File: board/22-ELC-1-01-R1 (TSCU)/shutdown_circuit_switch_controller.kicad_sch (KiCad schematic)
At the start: 28 parts, among them Q5 AO3400A, Q6 AO3400A, Q7 SUD50P04-09L-E3, Q8 SUD50P04-09L-E3, U11 SN74LVC1G14DBV, U12 74LS32, U3 74HC74D,653, U4 SGM809-SXN3/TR

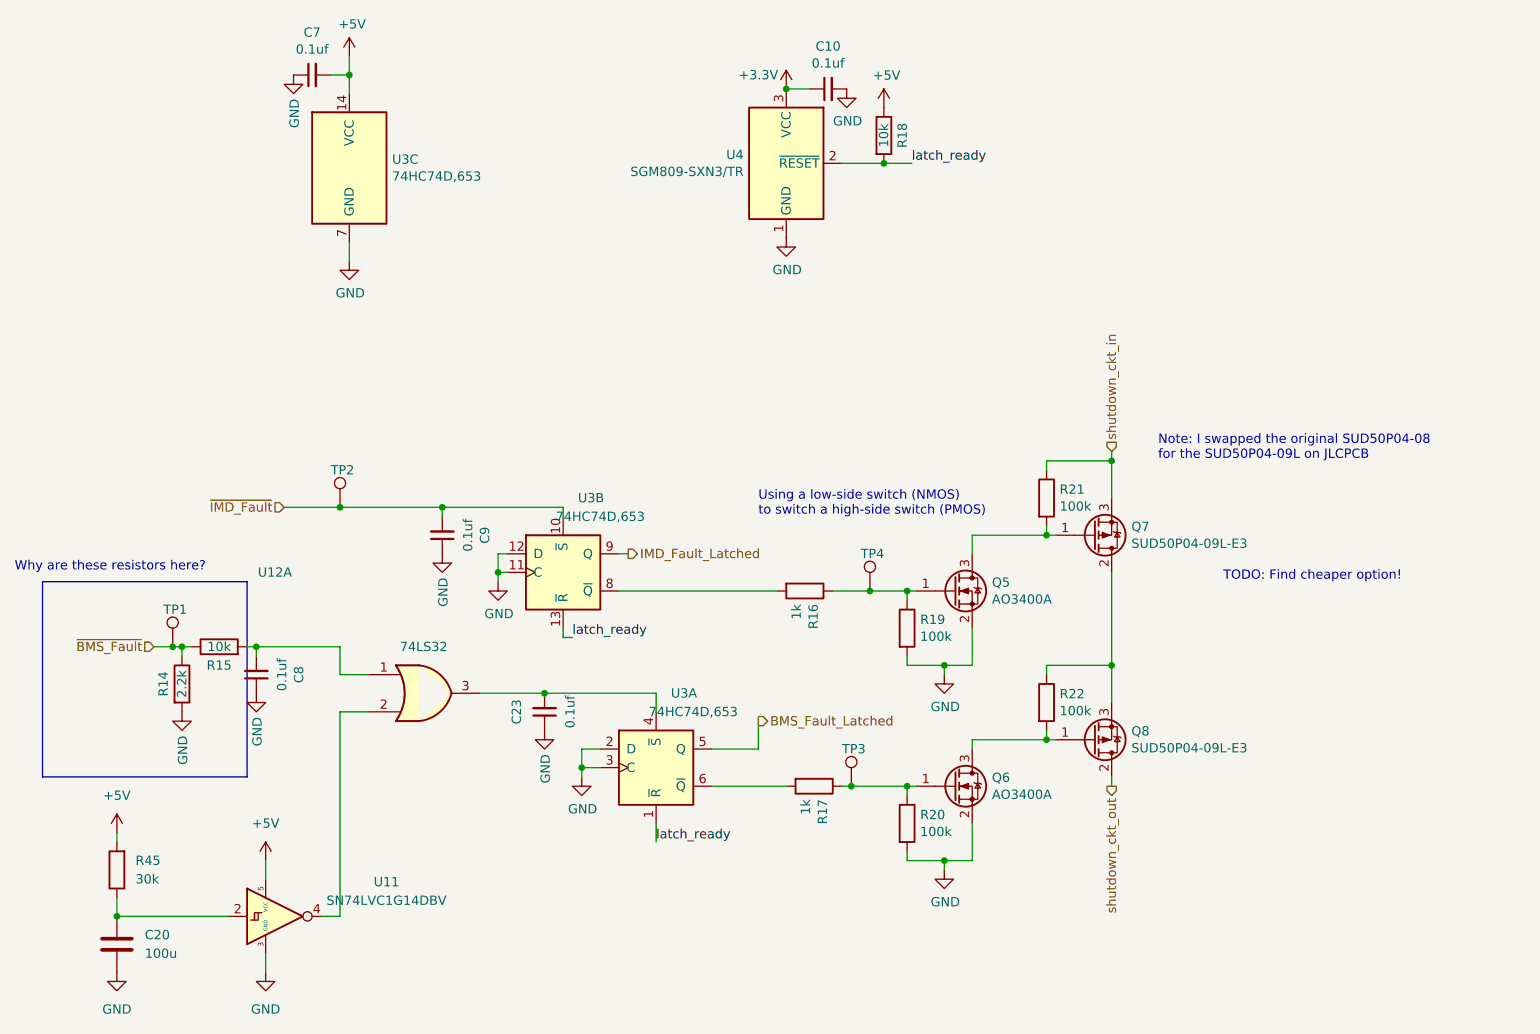
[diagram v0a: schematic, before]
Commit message: Added FAULT_RESET button
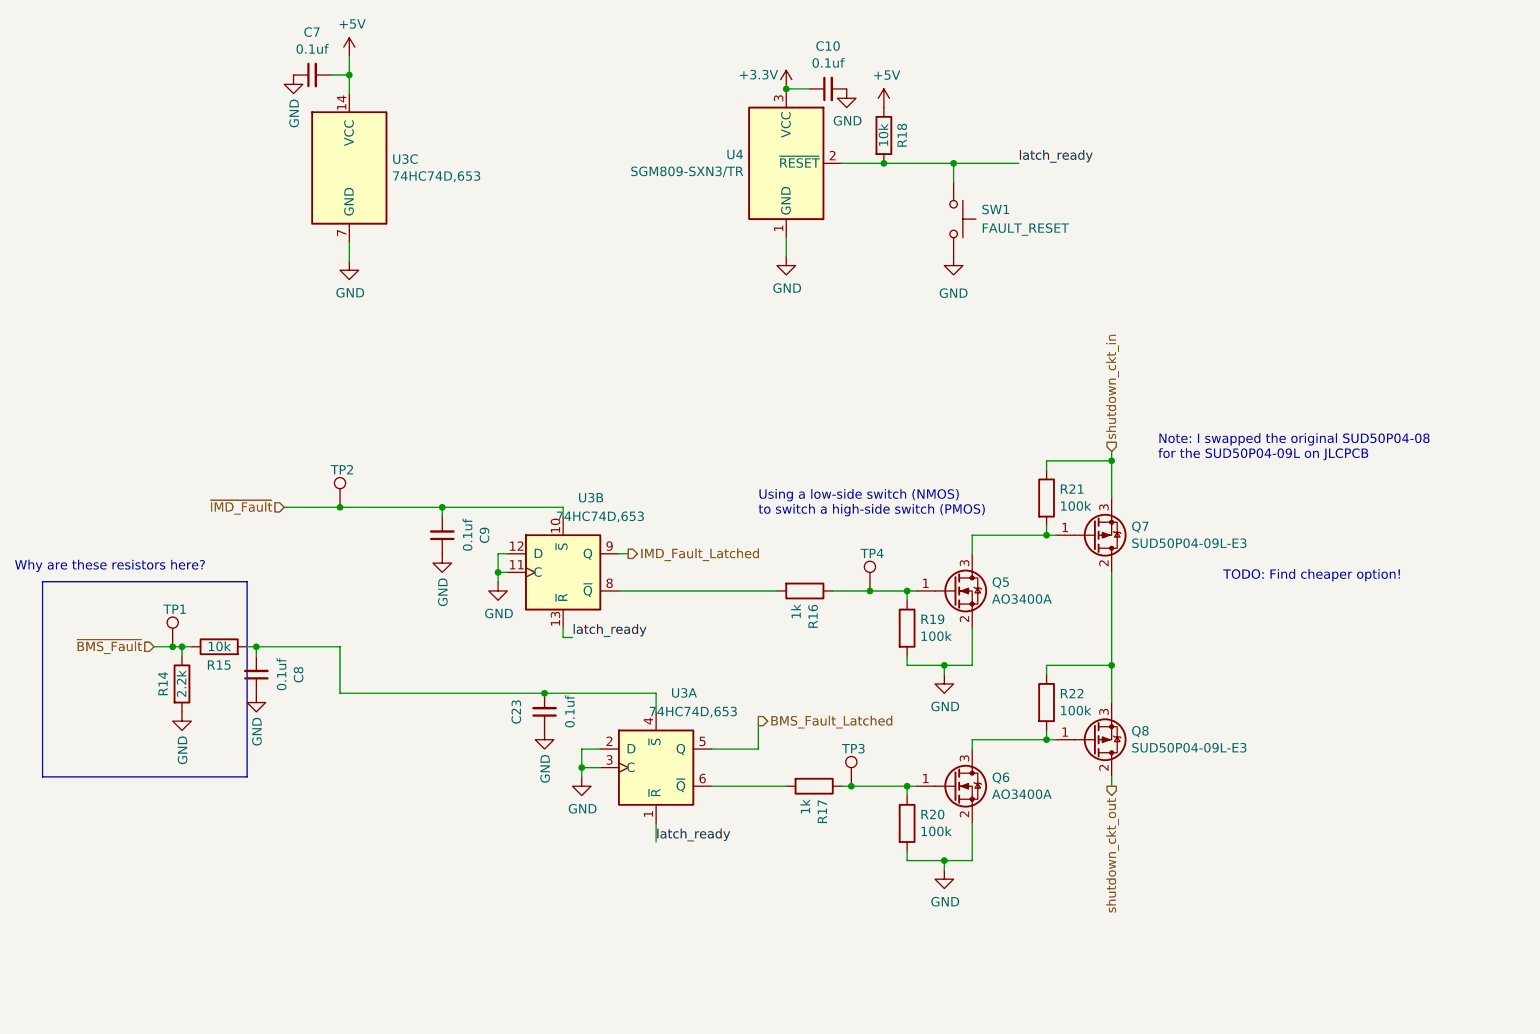
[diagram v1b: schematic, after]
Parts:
- removed C20: 100u, symbol Device:C
- removed R45: 30k, symbol Device:R
- removed U11: SN74LVC1G14DBV, Package_TO_SOT_SMD:SOT-23-5, symbol 74xGxx:SN74LVC1G14DBV
- removed U12: 74LS32, symbol 74xx:74LS32
- added SW1: FAULT_RESET, symbol Switch:SW_Push
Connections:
- net GND: now also SW1.2
- net latch_ready: now also SW1.1
- net at C8.2, R15.2: now also C23.2, U3.4 (~{S})

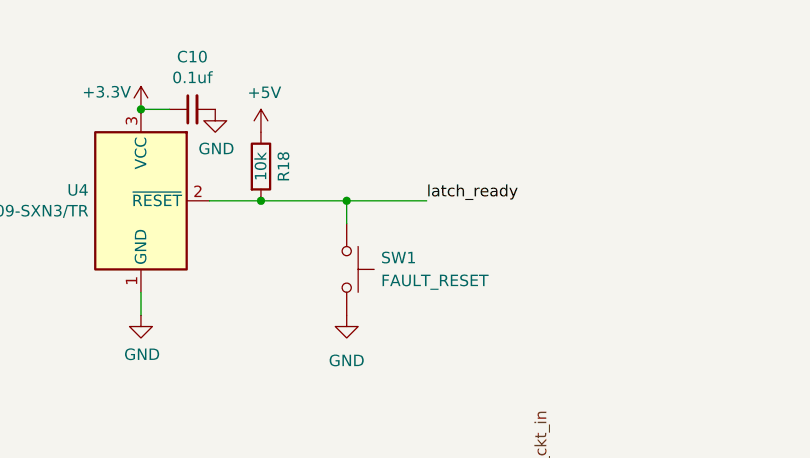
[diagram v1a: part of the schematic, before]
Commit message: Added few LEDs
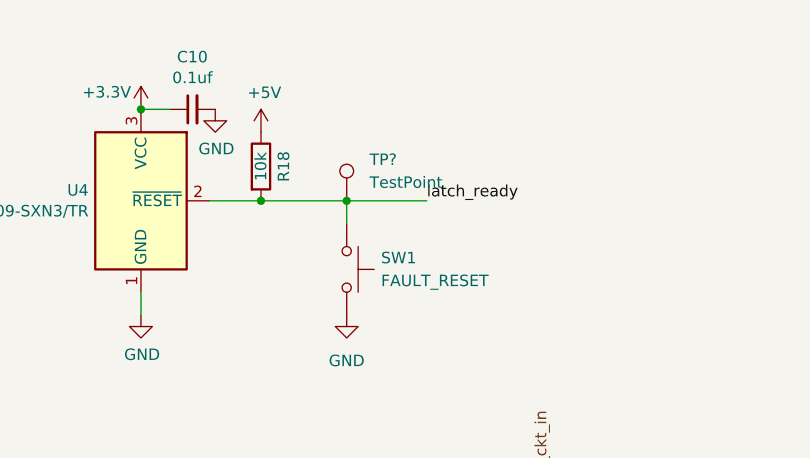
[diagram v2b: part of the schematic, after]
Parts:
- added TP?: TestPoint, symbol Connector:TestPoint
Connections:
- net latch_ready: now also TP?.1
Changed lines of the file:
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@@
+    (pin "1")
+  )
+  (symbol (lib_id "Connector:TestPoint") (at 139.7 49.53 0) (unit 1)
+    (in_bom yes) (on_board yes) (fields_autoplaced)
+    (property "Reference" "TP?" (id 0) (at 142.24 44.9579 0)
+      (effects (font (size 1.27 1.27)) (justify left))
+    )
+    (property "Value" "TestPoint" (id 1) (at 142.24 47.4979 0)
+      (effects (font (size 1.27 1.27)) (justify left))
+    )
+    (property "Footprint" "" (id 2) (at 144.78 49.53 0)
+      (effects (font (size 1.27 1.27)) hide)
+    )
+    (property "Datasheet" "~" (id 3) (at 144.78 49.53 0)
+      (effects (font (size 1.27 1.27)) hide)
+    )
     (pin "1")
   )

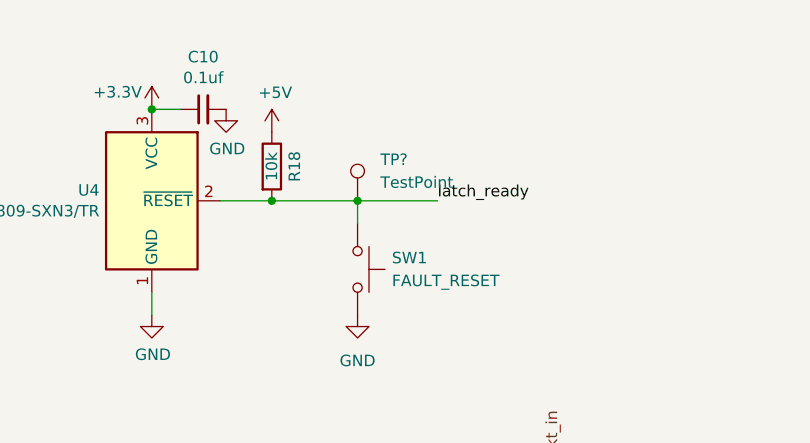
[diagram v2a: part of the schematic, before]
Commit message: More LEDs and test points
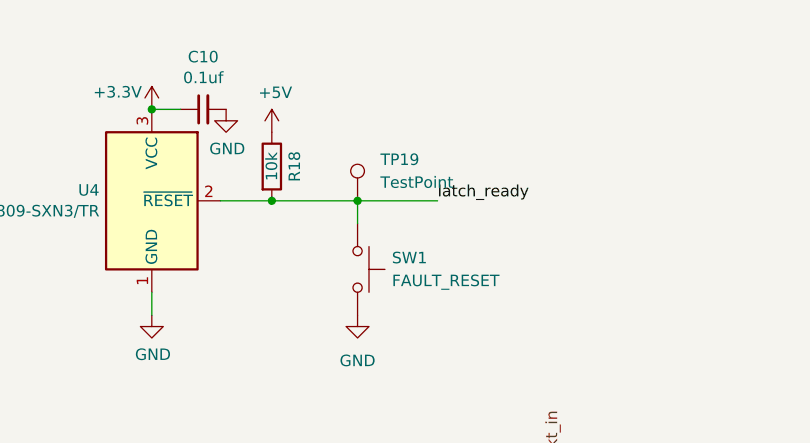
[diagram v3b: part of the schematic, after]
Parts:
- gave numbers to parts that had none: 1
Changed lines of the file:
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@@
   (symbol (lib_id "Connector:TestPoint") (at 139.7 49.53 0) (unit 1)
     (in_bom yes) (on_board yes) (fields_autoplaced)
-    (property "Reference" "TP?" (id 0) (at 142.24 44.9579 0)
+    (property "Reference" "TP19" (id 0) (at 142.24 44.9579 0)
       (effects (font (size 1.27 1.27)) (justify left))
     )

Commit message: Ready for review
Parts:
- renumbered C8 to C20, C7 to C21, C9 to C22, C10 to C24, Q6 to Q10, Q7 to Q11, Q8 to Q12, Q5 to Q9, R14 to R34, R15 to R35, R16 to R36, R17 to R37, R18 to R38, R19 to R39, R20 to R40, R21 to R41, R22 to R42, TP1 to TP15, TP2 to TP16, TP3 to TP17, TP4 to TP18, U3 to U7, U4 to U8

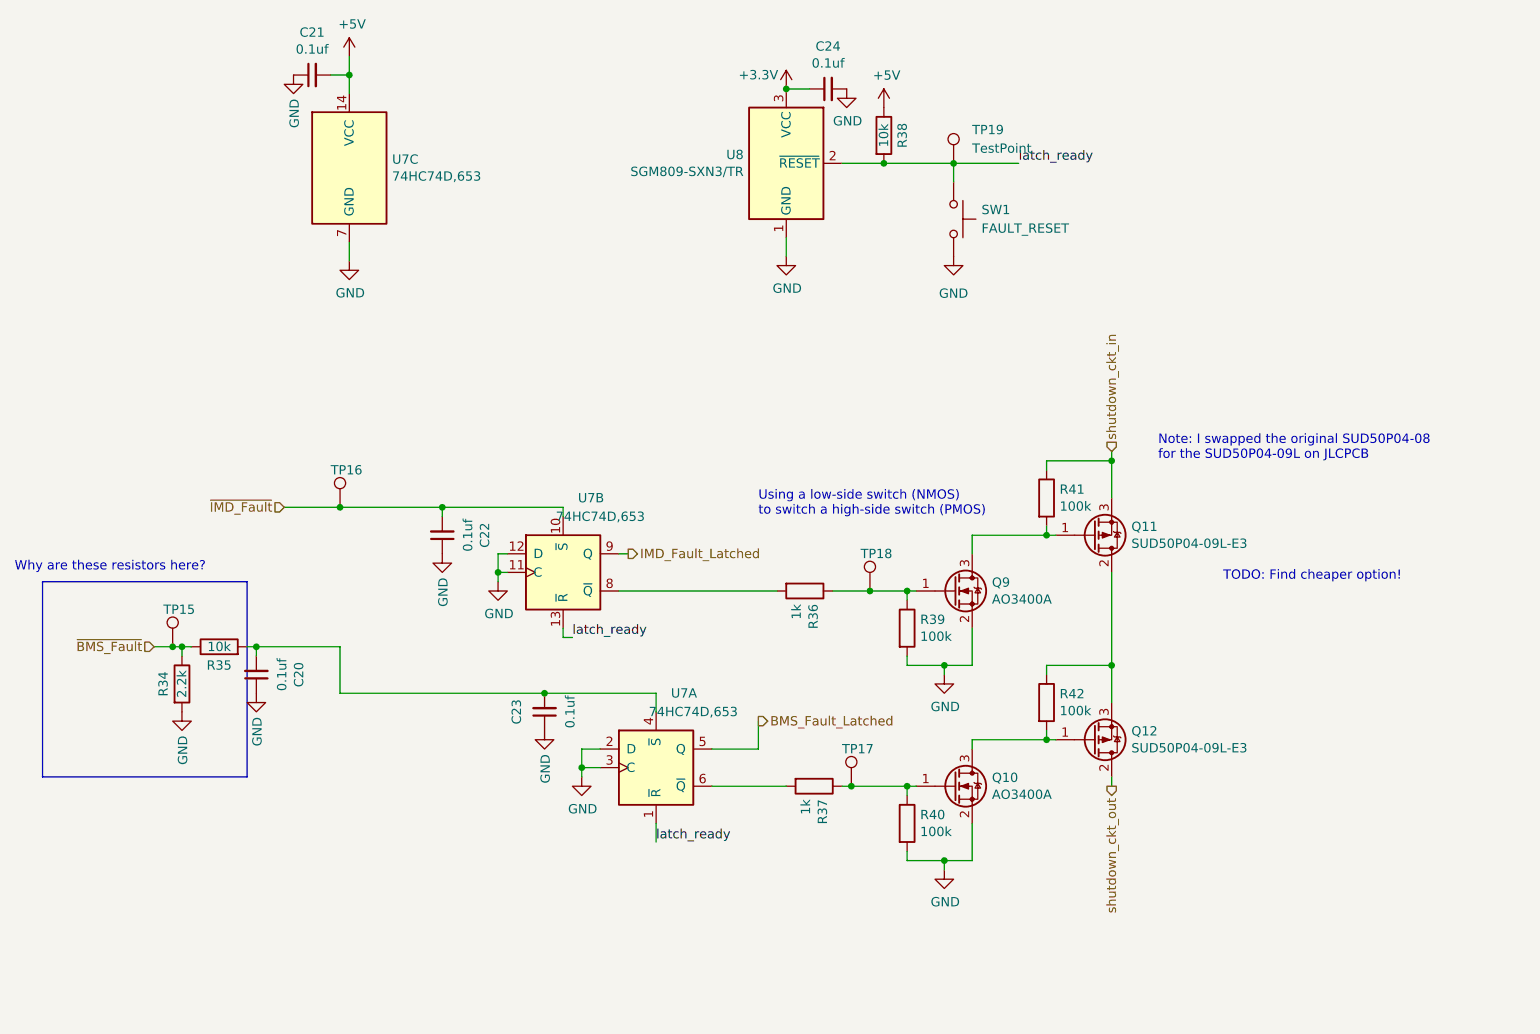
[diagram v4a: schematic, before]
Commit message: All good except need to switch everything to accepting 24v power
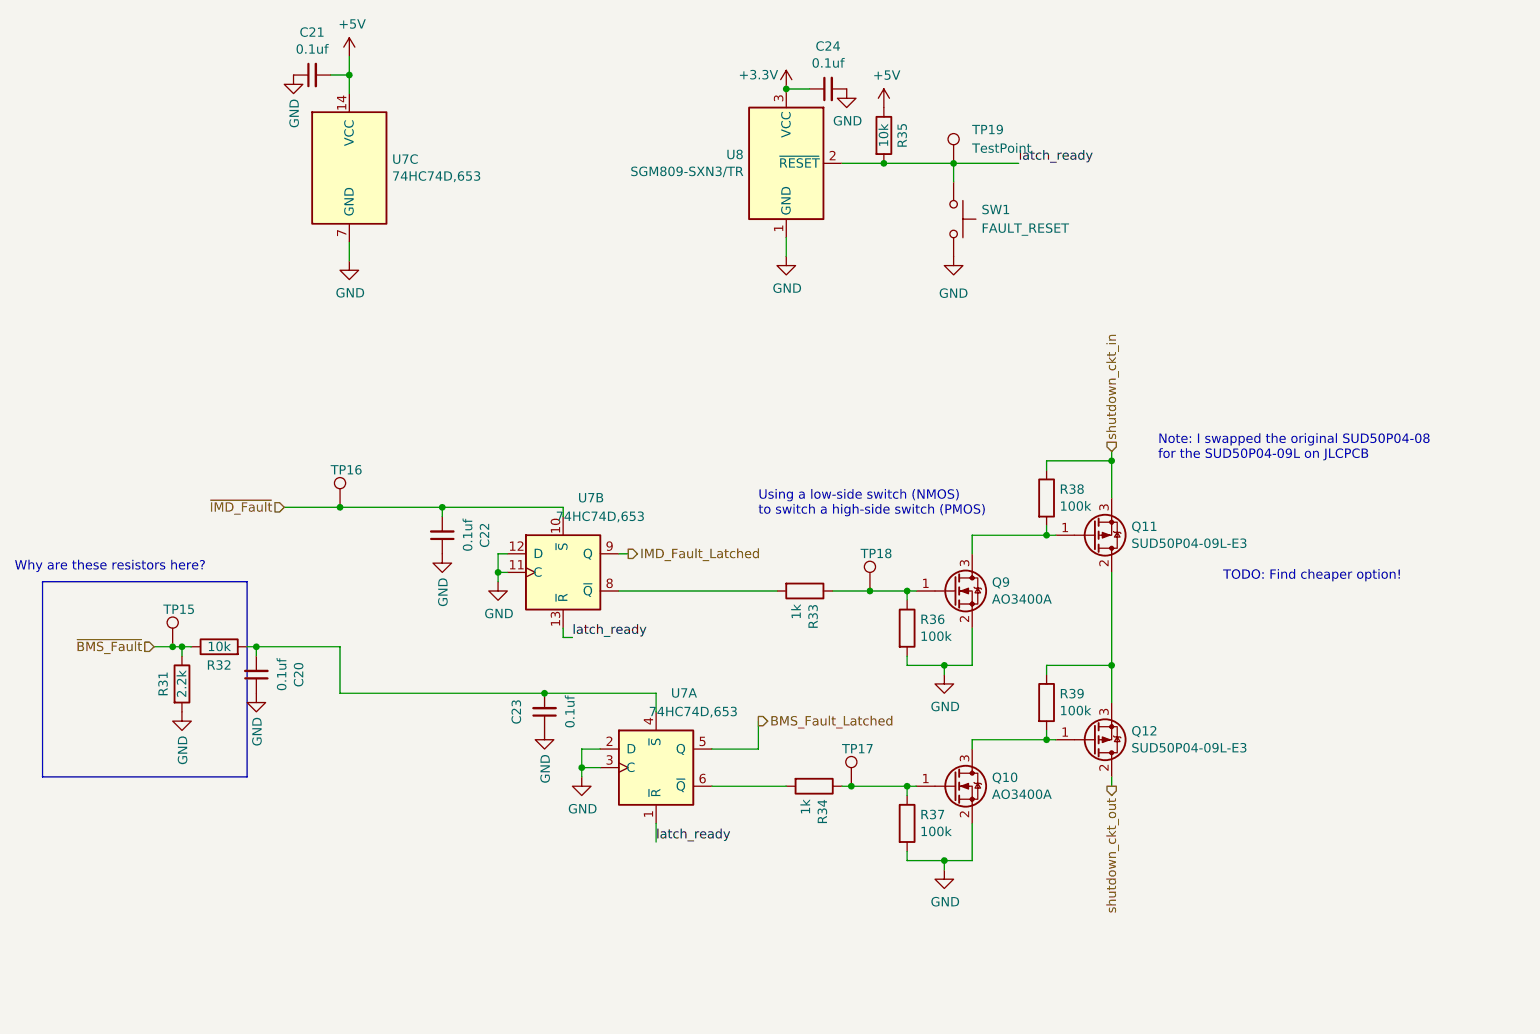
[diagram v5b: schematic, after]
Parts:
- SW1: footprint (none) -> Button_Switch_SMD:SW_DIP_SPSTx01_Slide_6.7x4.1mm_W8.61mm_P2.54mm_LowProfile
- TP19: footprint (none) -> TestPoint:TestPoint_THTPad_D1.0mm_Drill0.5mm
- renumbered R34 to R31, R35 to R32, R36 to R33, R37 to R34, R38 to R35, R39 to R36, R40 to R37, R41 to R38, R42 to R39
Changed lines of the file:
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@@
   (symbol (lib_id "Device:R") (at 39.37 115.57 90) (unit 1)
     (in_bom yes) (on_board yes)
-    (property "Reference" "R35" (id 0) (at 39.37 118.11 90))
+    (property "Reference" "R32" (id 0) (at 39.37 118.11 90))
     (property "Value" "10k" (id 1) (at 39.37 115.57 90))
     (property "Footprint" "Resistor_SMD:R_0603_1608Metric_Pad0.98x0.95mm_HandSolder" (id 2) (at 39.37 117.348 90)
@@
   (symbol (lib_id "Device:R") (at 34.29 120.65 0) (unit 1)
     (in_bom yes) (on_board yes)
-    (property "Reference" "R34" (id 0) (at 31.75 120.65 90))
+    (property "Reference" "R31" (id 0) (at 31.75 120.65 90))
     (property "Value" "2.2k" (id 1) (at 34.29 120.65 90))
     (property "Footprint" "Resistor_SMD:R_0603_1608Metric_Pad0.98x0.95mm_HandSolder" (id 2) (at 32.512 120.65 90)
@@
   (symbol (lib_id "Device:R") (at 152.4 95.25 0) (unit 1)
     (in_bom yes) (on_board yes)
-    (property "Reference" "R41" (id 0) (at 154.178 94.0816 0)
+    (property "Reference" "R38" (id 0) (at 154.178 94.0816 0)
       (effects (font (size 1.27 1.27)) (justify left))
     )
@@
   (symbol (lib_id "Device:R") (at 152.4 123.19 0) (unit 1)
     (in_bom yes) (on_board yes)
-    (property "Reference" "R42" (id 0) (at 154.178 122.0216 0)
+    (property "Reference" "R39" (id 0) (at 154.178 122.0216 0)
       (effects (font (size 1.27 1.27)) (justify left))
     )
@@
   (symbol (lib_id "Device:R") (at 133.35 113.03 0) (unit 1)
     (in_bom yes) (on_board yes)
-    (property "Reference" "R39" (id 0) (at 135.128 111.8616 0)
+    (property "Reference" "R36" (id 0) (at 135.128 111.8616 0)
       (effects (font (size 1.27 1.27)) (justify left))
     )
@@
   (symbol (lib_id "Device:R") (at 133.35 139.7 0) (unit 1)
     (in_bom yes) (on_board yes)
-    (property "Reference" "R40" (id 0) (at 135.128 138.5316 0)
+    (property "Reference" "R37" (id 0) (at 135.128 138.5316 0)
       (effects (font (size 1.27 1.27)) (justify left))
     )
@@
   (symbol (lib_id "Device:R") (at 130.175 45.72 0) (unit 1)
     (in_bom yes) (on_board yes)
-    (property "Reference" "R38" (id 0) (at 132.715 45.72 90))
+    (property "Reference" "R35" (id 0) (at 132.715 45.72 90))
     (property "Value" "10k" (id 1) (at 130.175 45.72 90))
     (property "Footprint" "Resistor_SMD:R_0603_1608Metric_Pad0.98x0.95mm_HandSolder" (id 2) (at 128.397 45.72 90)
@@
   (symbol (lib_id "Device:R") (at 119.38 107.95 270) (unit 1)
     (in_bom yes) (on_board yes)
-    (property "Reference" "R36" (id 0) (at 120.5484 109.728 0)
+    (property "Reference" "R33" (id 0) (at 120.5484 109.728 0)
       (effects (font (size 1.27 1.27)) (justify left))
     )
@@
   (symbol (lib_id "Device:R") (at 120.65 134.62 270) (unit 1)
     (in_bom yes) (on_board yes)
-    (property "Reference" "R37" (id 0) (at 121.8184 136.398 0)
+    (property "Reference" "R34" (id 0) (at 121.8184 136.398 0)
       (effects (font (size 1.27 1.27)) (justify left))
     )
@@
       (effects (font (size 1.27 1.27)) (justify left))
     )
-    (property "Footprint" "" (id 2) (at 144.78 57.15 0)
+    (property "Footprint" "Button_Switch_SMD:SW_DIP_SPSTx01_Slide_6.7x4.1mm_W8.61mm_P2.54mm_LowProfile" (id 2) (at 144.78 57.15 0)
       (effects (font (size 1.27 1.27)) hide)
     )
@@
       (effects (font (size 1.27 1.27)) (justify left))
     )
-    (property "Footprint" "" (id 2) (at 144.78 49.53 0)
-      (effects (font (size 1.27 1.27)) hide)
-    )
+    (property "Footprint" "TestPoint:TestPoint_THTPad_D1.0mm_Drill0.5mm" (id 2) (at 144.78 49.53 0)
+      (effects (font (size 1.27 1.27)) hide)
+    )
